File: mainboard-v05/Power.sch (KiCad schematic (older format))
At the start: 70 parts, among them J14 Conn_01x06, Q1 IRLML2803, Q2 MBT2222ADW1T1, Q22 NDS8434, Q3 MBT2222ADW1T1, U17 BQ25883RGER, U21 TPS7A4501DCQT, U4 ADM1176-1ARMZ-R7, U5 TPS54226PWPRPWP14_2P31X2P46-L, U6 LTC4121, U7 KF50BD-TR

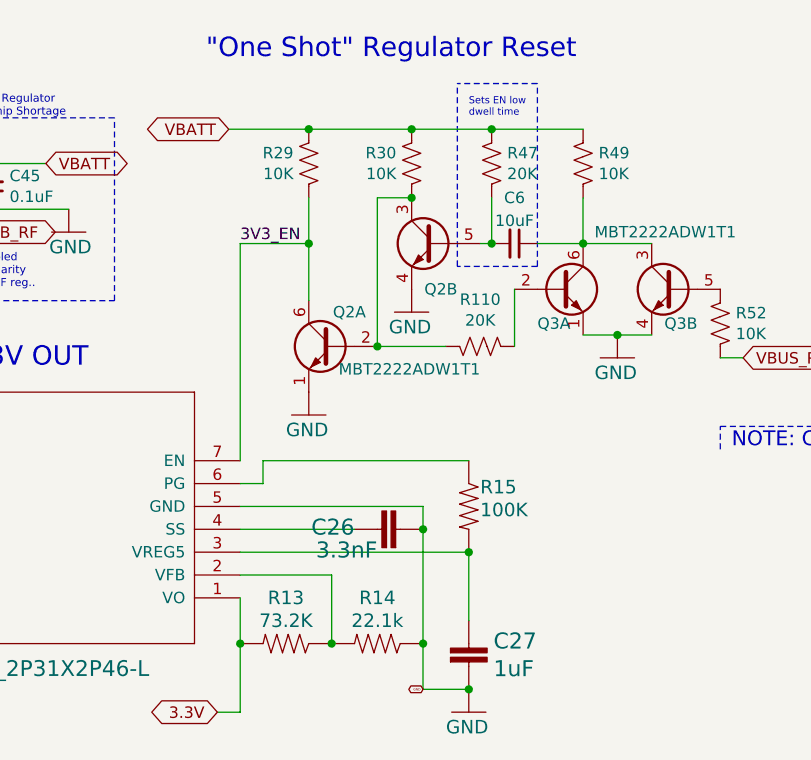
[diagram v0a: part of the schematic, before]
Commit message: tweaking one-shot values for reduced power consumption
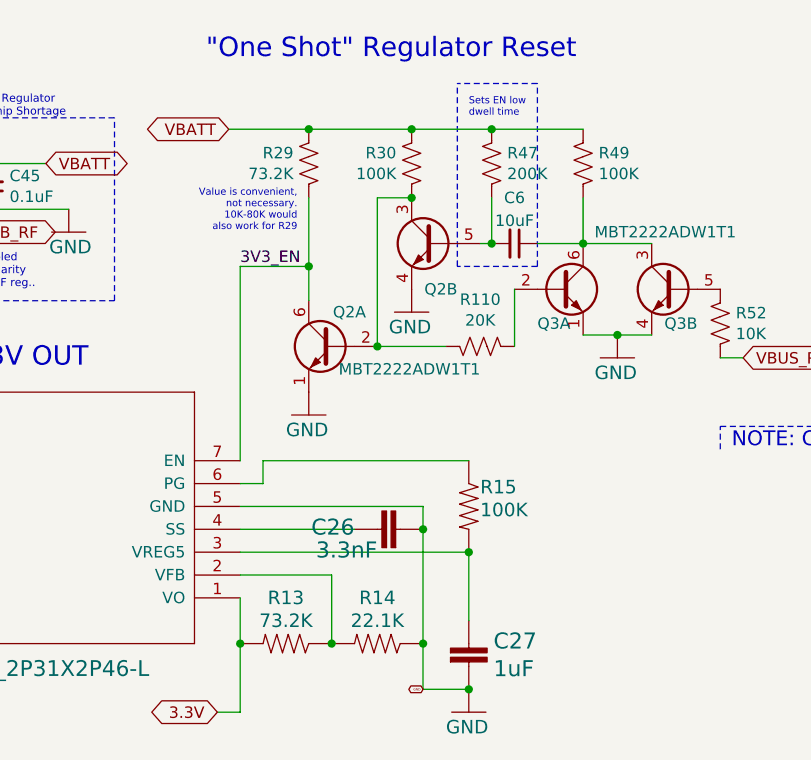
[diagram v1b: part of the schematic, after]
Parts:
- R14: value 22.1k -> 22.1K; Description 22.1k 0603 -> 22.1K 0603
- R29: value 10K -> 73.2K; Description 10K 0603 -> 73.2K 0603
- R30, R49: value 10K -> 100K; Description 10K 0603 -> 100K 0603
- R47: value 20K -> 200K; Description 20K 0603 -> 200K 0603
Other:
- note added: "Value is convenient,\nnot necessary. \n10K-80K would\nalso work for R29"
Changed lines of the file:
@@
 AR Path="/5CEC5DDE/07A6364C" Ref="R14"  Part="1"
 F 0 "R14" H 5450 7150 59  0000 C CNN
-F 1 "22.1k" H 5450 7250 59  0000 C CNN
+F 1 "22.1K" H 5450 7250 59  0000 C CNN
 F 2 "Resistor_SMD:R_0603_1608Metric" H 5450 7350 50  0001 C CNN
 F 3 "" H 5450 7350 50  0001 C CNN
-F 4 "22.1k 0603" H 5450 7250 50  0001 C CNN "Description"
+F 4 "22.1K 0603" H 5450 7250 50  0001 C CNN "Description"
 	1    5450 7350
 	-1   0    0    1
@@
 AR Path="/5CEC5DDE/5F1B44AB" Ref="R49"  Part="1"
 F 0 "R49" H 6282 5296 50  0000 R CNN
-F 1 "10K" H 6282 5205 50  0000 R CNN
+F 1 "100K" H 6282 5205 50  0000 R CNN
 F 2 "Resistor_SMD:R_0603_1608Metric" V 6390 5240 50  0001 C CNN
 F 3 "" H 6350 5250 50  0001 C CNN
-F 4 "10K 0603" H 6282 5396 50  0001 C CNN "Description"
+F 4 "100K 0603" H 6282 5396 50  0001 C CNN "Description"
 	1    6350 5250
 	-1   0    0    -1
@@
 AR Path="/5CEC5DDE/5F1CA9D3" Ref="R47"  Part="1"
 F 0 "R47" H 5882 5296 50  0000 R CNN
-F 1 "20K" H 5882 5205 50  0000 R CNN
+F 1 "200K" H 5882 5205 50  0000 R CNN
 F 2 "Resistor_SMD:R_0603_1608Metric" V 5990 5240 50  0001 C CNN
 F 3 "" H 5950 5250 50  0001 C CNN
-F 4 "20K 0603" H 5882 5396 50  0001 C CNN "Description"
+F 4 "200K 0603" H 5882 5396 50  0001 C CNN "Description"
 	1    5950 5250
 	-1   0    0    -1
@@
 AR Path="/5CEC5DDE/5F1EA9B1" Ref="R30"  Part="1"
 F 0 "R30" H 5667 5296 50  0000 L CNN
-F 1 "10K" H 5667 5205 50  0000 L CNN
+F 1 "100K" H 5667 5205 50  0000 L CNN
 F 2 "Resistor_SMD:R_0603_1608Metric" V 5640 5240 50  0001 C CNN
 F 3 "" H 5600 5250 50  0001 C CNN
-F 4 "10K 0603" H 5667 5396 50  0001 C CNN "Description"
+F 4 "100K 0603" H 5667 5396 50  0001 C CNN "Description"
 	1    5600 5250
 	-1   0    0    -1
@@
 AR Path="/5CEC5DDE/5F203452" Ref="R29"  Part="1"
 F 0 "R29" H 5217 5296 50  0000 L CNN
-F 1 "10K" H 5217 5205 50  0000 L CNN
+F 1 "73.2K" H 5217 5205 50  0000 L CNN
 F 2 "Resistor_SMD:R_0603_1608Metric" V 5190 5240 50  0001 C CNN
 F 3 "" H 5150 5250 50  0001 C CNN
-F 4 "10K 0603" H 5217 5396 50  0001 C CNN "Description"
+F 4 "73.2K 0603" H 5217 5396 50  0001 C CNN "Description"
 	1    5150 5250
 	-1   0    0    -1
@@
 Text GLabel 8150 4750 0    50   Input ~ 0
 SCL_PWR
-Text Label 4850 5600 0    50   ~ 0
+Text Label 4850 5700 0    50   ~ 0
 3V3_EN
 Text GLabel 4800 5100 0    50   BiDi ~ 0
@@
 	5950 5100 6350 5100
 Wire Wire Line
-	5150 5400 5150 5600
-Wire Wire Line
-	4850 6550 4850 5600
-Wire Wire Line
-	4850 5600 5150 5600
-Wire Wire Line
-	5150 5600 5150 5850
+	5150 5400 5150 5700
+Wire Wire Line
+	4850 6550 4850 5700
+Wire Wire Line
+	4850 5700 5150 5700
+Wire Wire Line
+	5150 5700 5150 5850
 Wire Wire Line
 	5600 5100 5950 5100
@@
 Connection ~ 5600 5100
 Connection ~ 5950 5100
-Connection ~ 5150 5600
+Connection ~ 5150 5700
 Connection ~ 5150 5100
 Connection ~ 5950 5600
@@
 Text Notes 3500 5800 0    35   ~ 0
 LOW = enabled\nOpposite polarity\nthan other RF reg..
+Text Notes 5100 5550 2    31   ~ 0
+Value is convenient,\nnot necessary. \n10K-80K would\nalso work for R29
 $EndSCHEMATC
